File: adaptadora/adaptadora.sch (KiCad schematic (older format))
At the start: 34 parts

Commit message: add files, libs, sch videos, sch sincronismo
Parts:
- removed C? (x8): 100n, symbol Device:C
- removed J? (x4): Conn_01x32_MountingPin, symbol Connector_Generic_MountingPin:Conn_01x32_MountingPin
- removed J?: Conn_02x10_Odd_Even, symbol Connector_Generic:Conn_02x10_Odd_Even
- removed JP? (x8): SolderJumper_3_Open, symbol Jumper:SolderJumper_3_Open
- removed RN? (x2): CAT16-153J8LF, CAT16104J4LF, symbol adaptadora-rescue:CAT16-153J8LF-CAT16-153J8LF
- removed U? (x4): SN74LVC2T45DCTR, DCT8, symbol adaptadora-rescue:SN74LVC2T45DCTR-2019-09-10_15-53-16-SH-rescue
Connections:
- net labels removed: ALT_0, ALT_1, ALT_2, ALT_3, ALT_4, ALT_5, ALT_6, ALT_7, GO_PULSE, PBRES, PBRES_EDU-CIAA, SPARE_1, SPARE_2, TIMEMARK, TIMEMARK_EDU-CIAA, TRIGG_SEC, TXA, TXA_EDU-CIAA, VIDEO_COMP, VIDEO_PRIM, ZRT
- wire segments 58 -> 0
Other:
- note removed: "FATA LO QUE VA A LA FPGA"
- note removed: "GPS"
- note removed: "LO DE ESTE LADO VA AL uC"
- note removed: "PE1A"
- note removed: "PE1B"
- note removed: "PE2A"
- note removed: "PE2B"
- note removed: "PEINE96"
- note removed: "TRANSLATORS"
- moved on the sheet: J?

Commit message: add files
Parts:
- removed J?: Conn_02x17_Odd_Even, symbol Connector_Generic:Conn_02x17_Odd_Even
- added C? (x7): C, symbol Device:C
- added C? (x4): CP1, symbol Device:CP1
- added D? (x3): D_TVS, symbol Device:D_TVS
- added J? (x7): Conn_Coaxial, symbol Connector:Conn_Coaxial
- added JP? (x4): Jumper_3_Open, symbol Jumper:Jumper_3_Open
- added R? (x3): R, symbol Device:R
- added RV? (x4): R_POT, symbol Device:R_POT
- added U?: TLV2772IDR, SOIC127P600X175-8N, symbol TLV2772IDR:TLV2772IDR
- added U?: LM361MX_NOPB-LM361MX_NOPB, SOIC127P600X175-14N, symbol sincronismo-rescue:LM361MX_NOPB-LM361MX_NOPB
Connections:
- net labels added: +12V, +5V, -12V, ACP_3P3, ARP_3P3, PRF_3P3, VIDEO_DIGITAL, V_COMP, V_COMP_3P3
- net labels removed: ACP, ACP_FPGA, ARP, ARP_FPGA, JMP1_FPGA, JMP2_FPGA, JMP3_FPGA, JMP4_FPGA, JMP5_FPGA, JMP6_FPGA, JMP7_FPGA, JMP8_FPGA, PRF, PRF_FPGA, VIDEO_COMP_FPGA, VIDEO_PRIM_FPGA
- wire segments 0 -> 144
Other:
- note removed: "DAC"
- note removed: "EDU-CIAA"
- note removed: "FALTA LA HUELLA DE LOS CAPACITORES Y LAS HUELLAS DE TODO NOMAS"
- note removed: "FPGA"
- moved on the sheet: J?

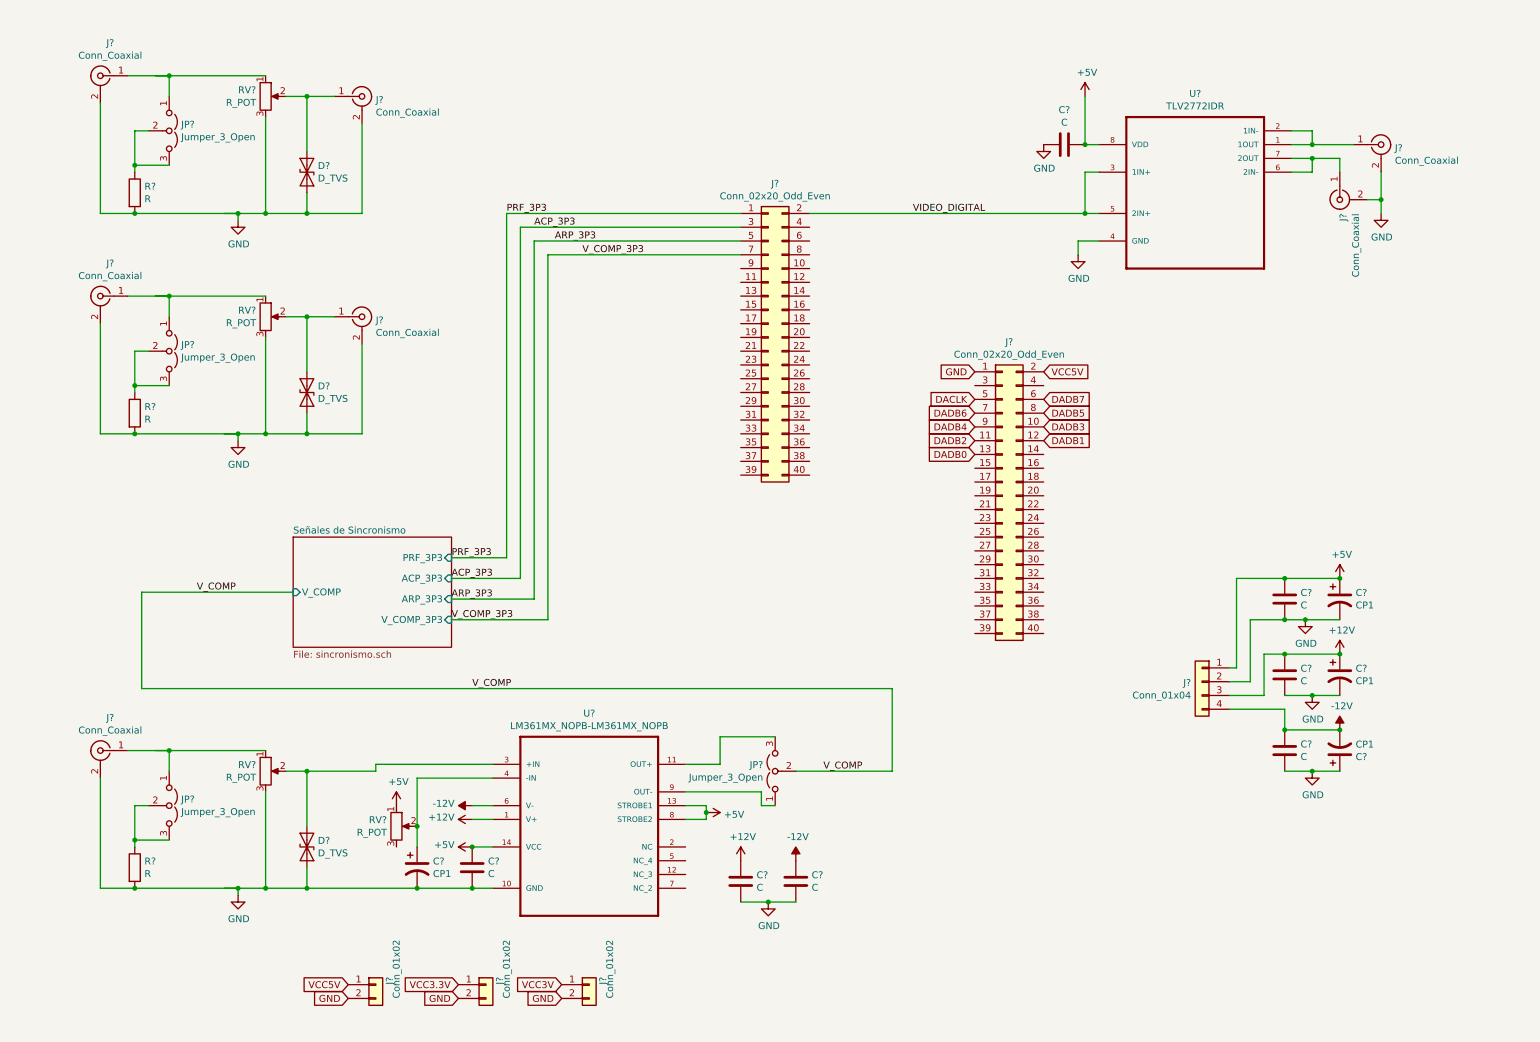
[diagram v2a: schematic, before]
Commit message: esquemático terminado faltan valores
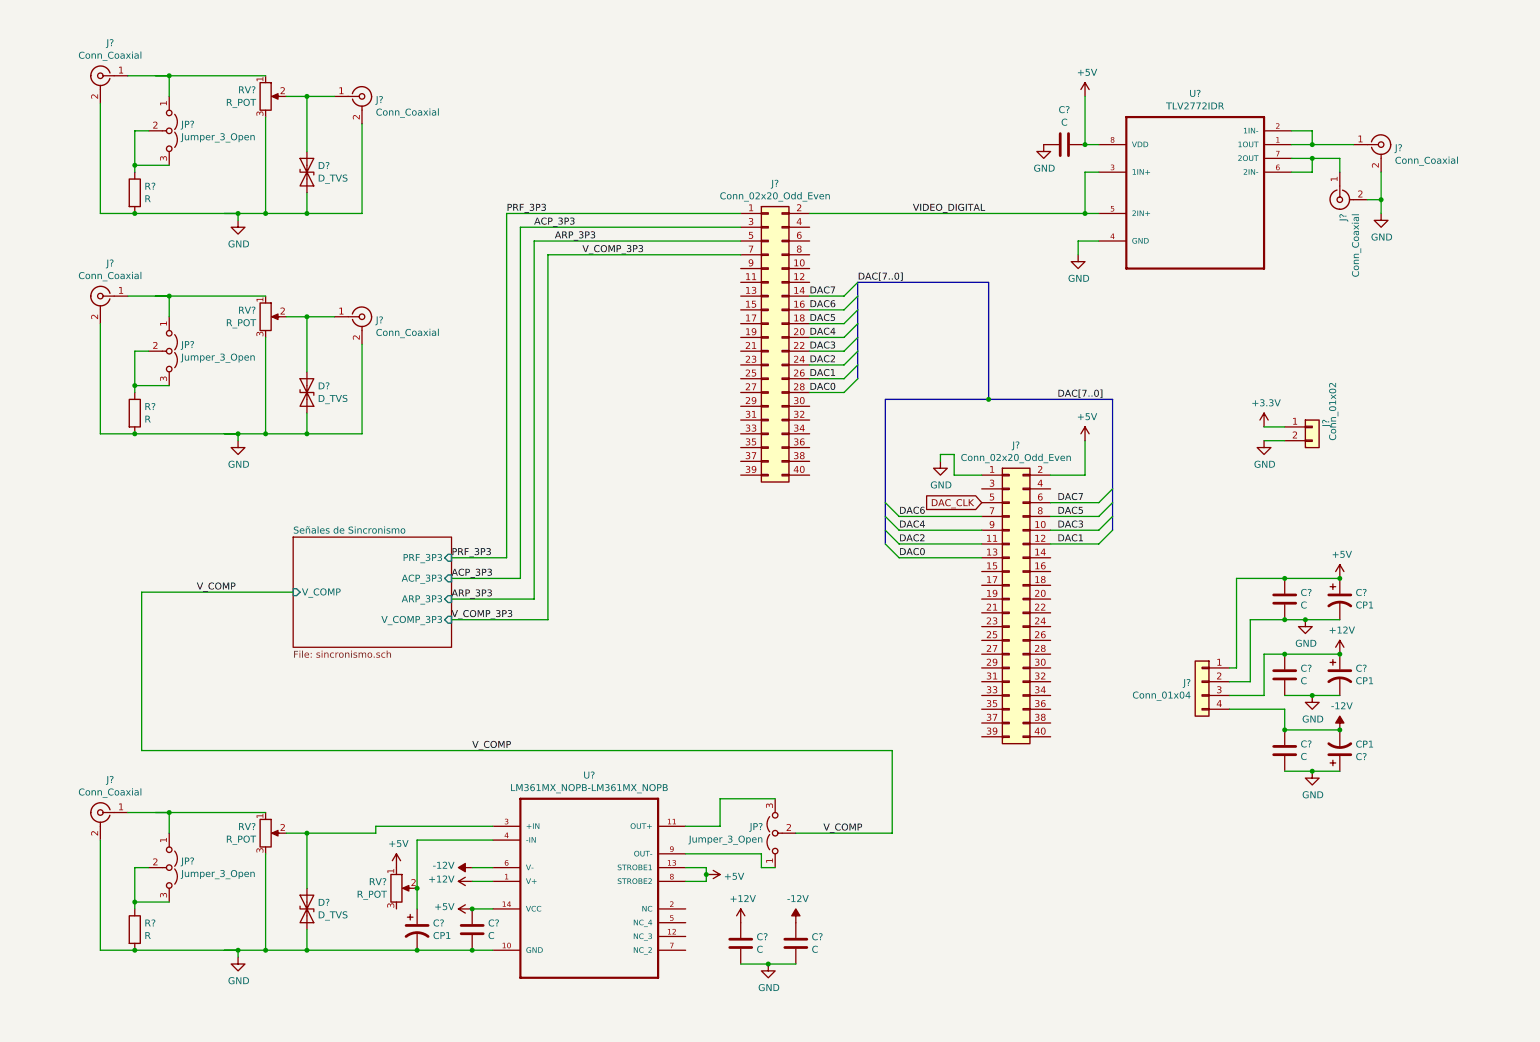
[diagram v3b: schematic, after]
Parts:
- removed J? (x2): Conn_01x02, symbol Connector_Generic:Conn_01x02
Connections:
- net labels added: +3.3V, DAC0, DAC1, DAC2, DAC3, DAC4, DAC5, DAC6, DAC7, DAC[7..0], DAC_CLK
- net labels removed: DACLK, DADB0, DADB1, DADB2, DADB3, DADB4, DADB5, DADB6, DADB7, VCC3.3V, VCC3V, VCC5V
- wire segments 144 -> 168
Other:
- moved on the sheet: C?, D?, J?, JP?, R?, RV?, U?

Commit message: se enumeraron componentes faltan valores
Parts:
- added J6: Conn_01x02, symbol Connector_Generic:Conn_01x02
- gave numbers to parts that had none: 38
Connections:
- wire segments 168 -> 173

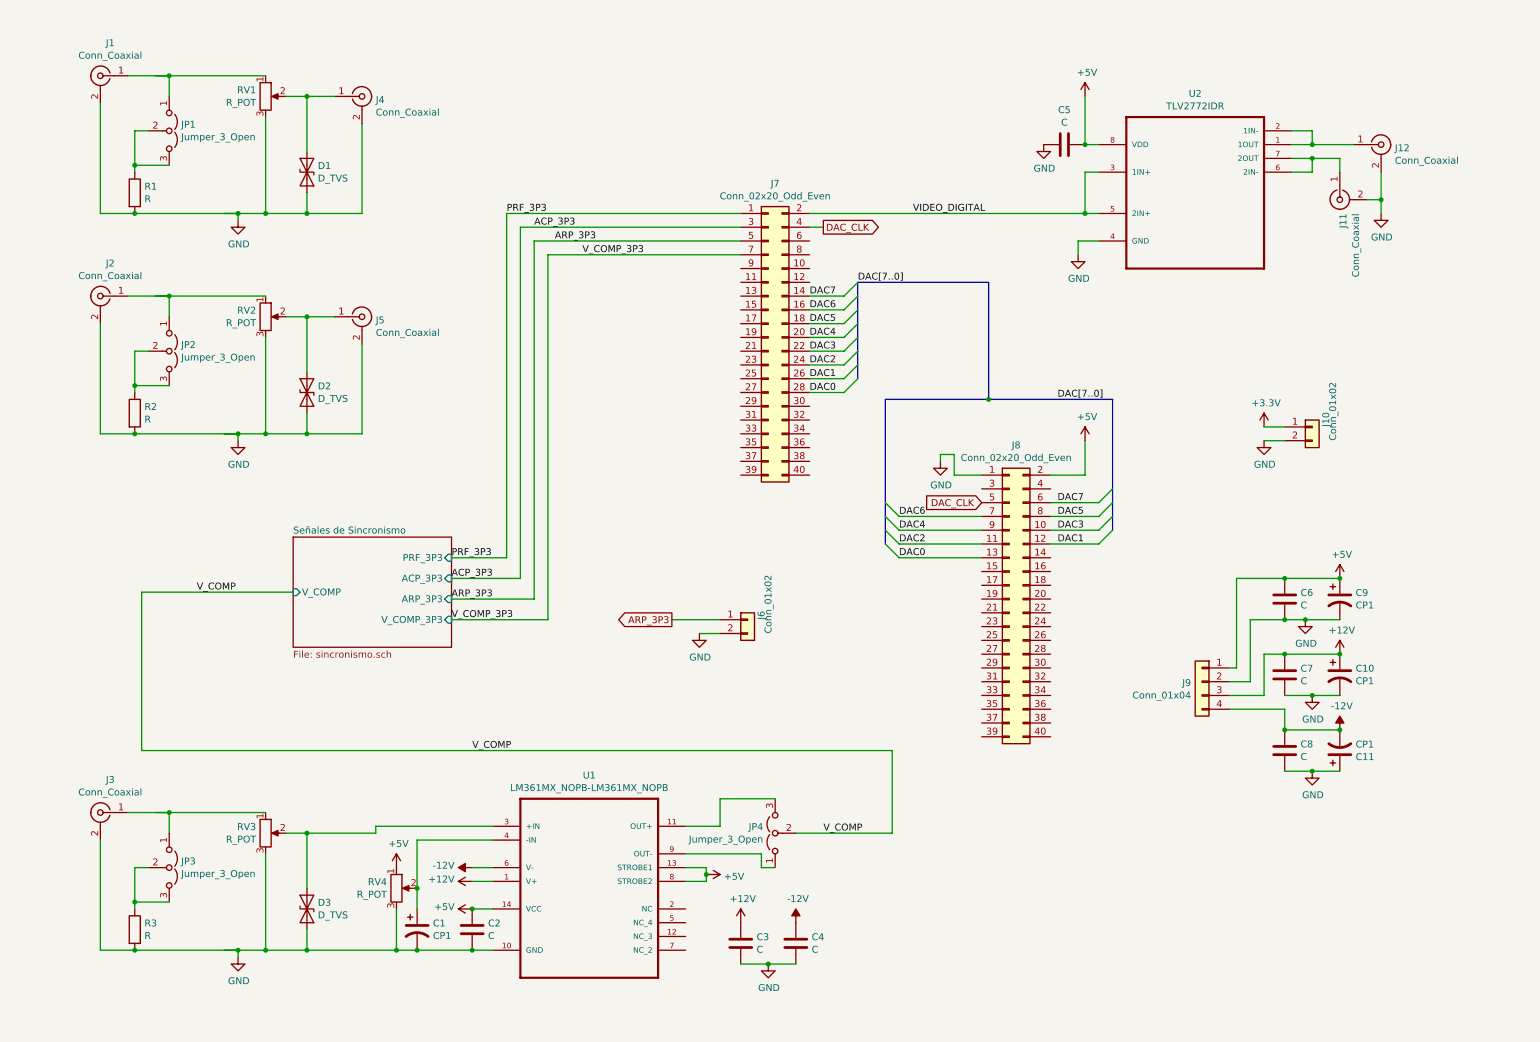
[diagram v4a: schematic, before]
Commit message: se agregan valores, etiquetas jerarquicas y poligonos
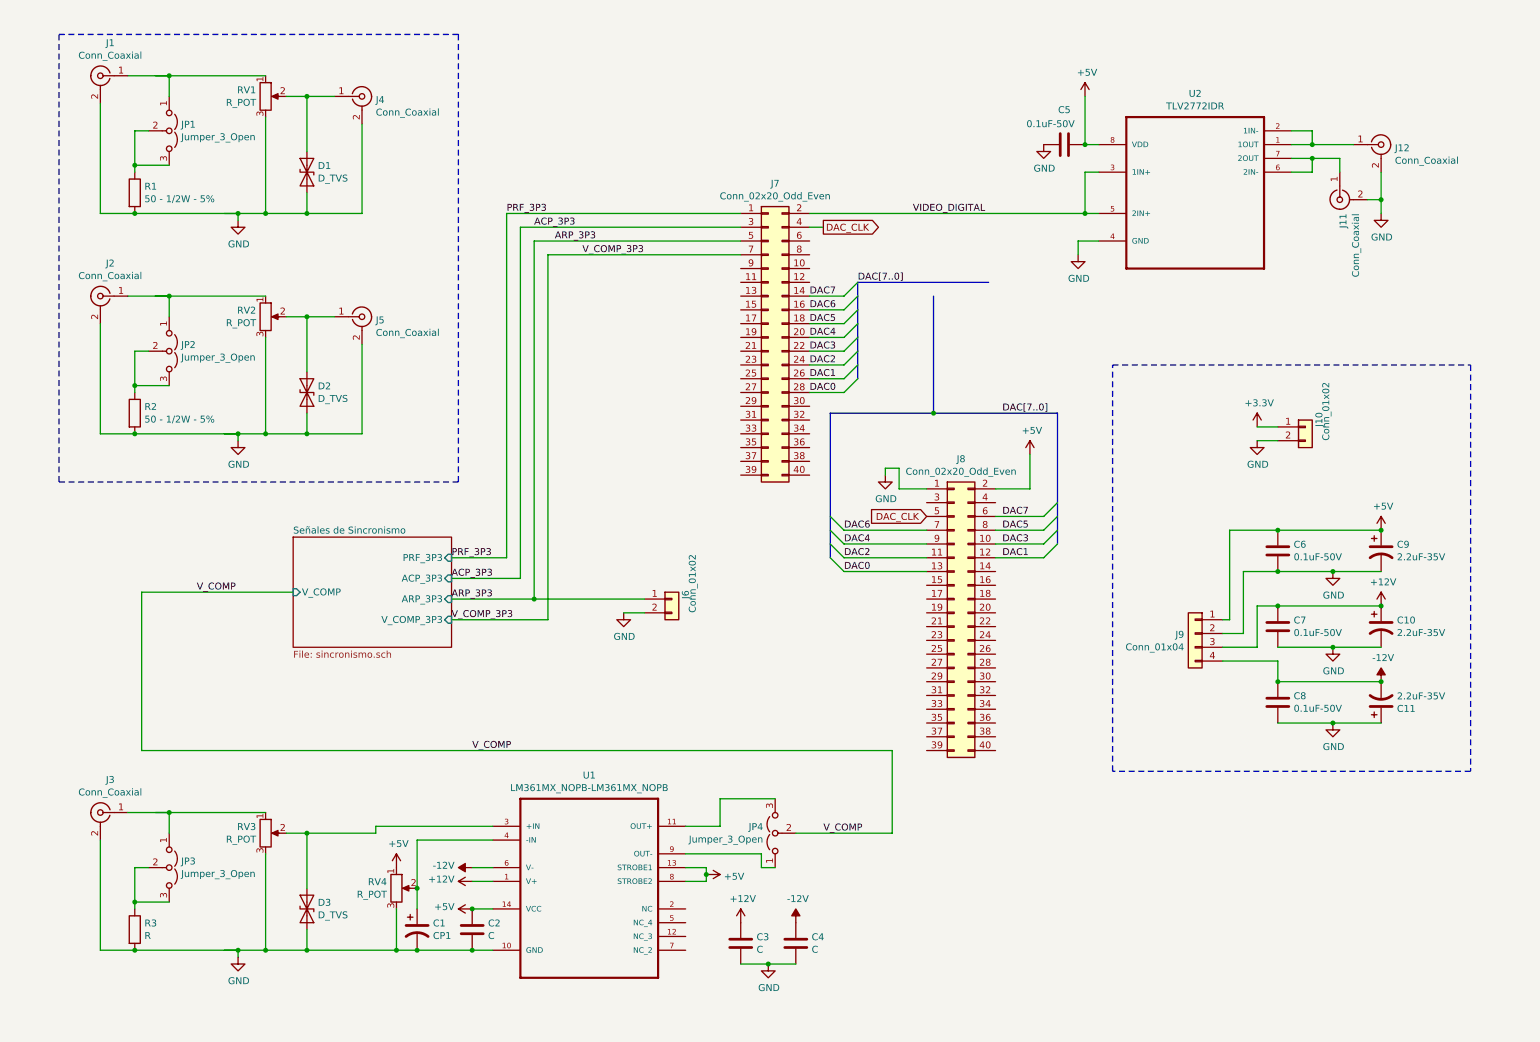
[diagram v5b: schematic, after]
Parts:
- C10, C11, C9: value CP1 -> 2.2uF-35V
- C5, C6, C7, C8: value C -> 0.1uF-50V
- R1, R2: value R -> 50 - 1/2W - 5%
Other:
- moved on the sheet: C10, C11, C6, C7, C8, C9, J10, J6, J8, J9

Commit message: se agrega texto
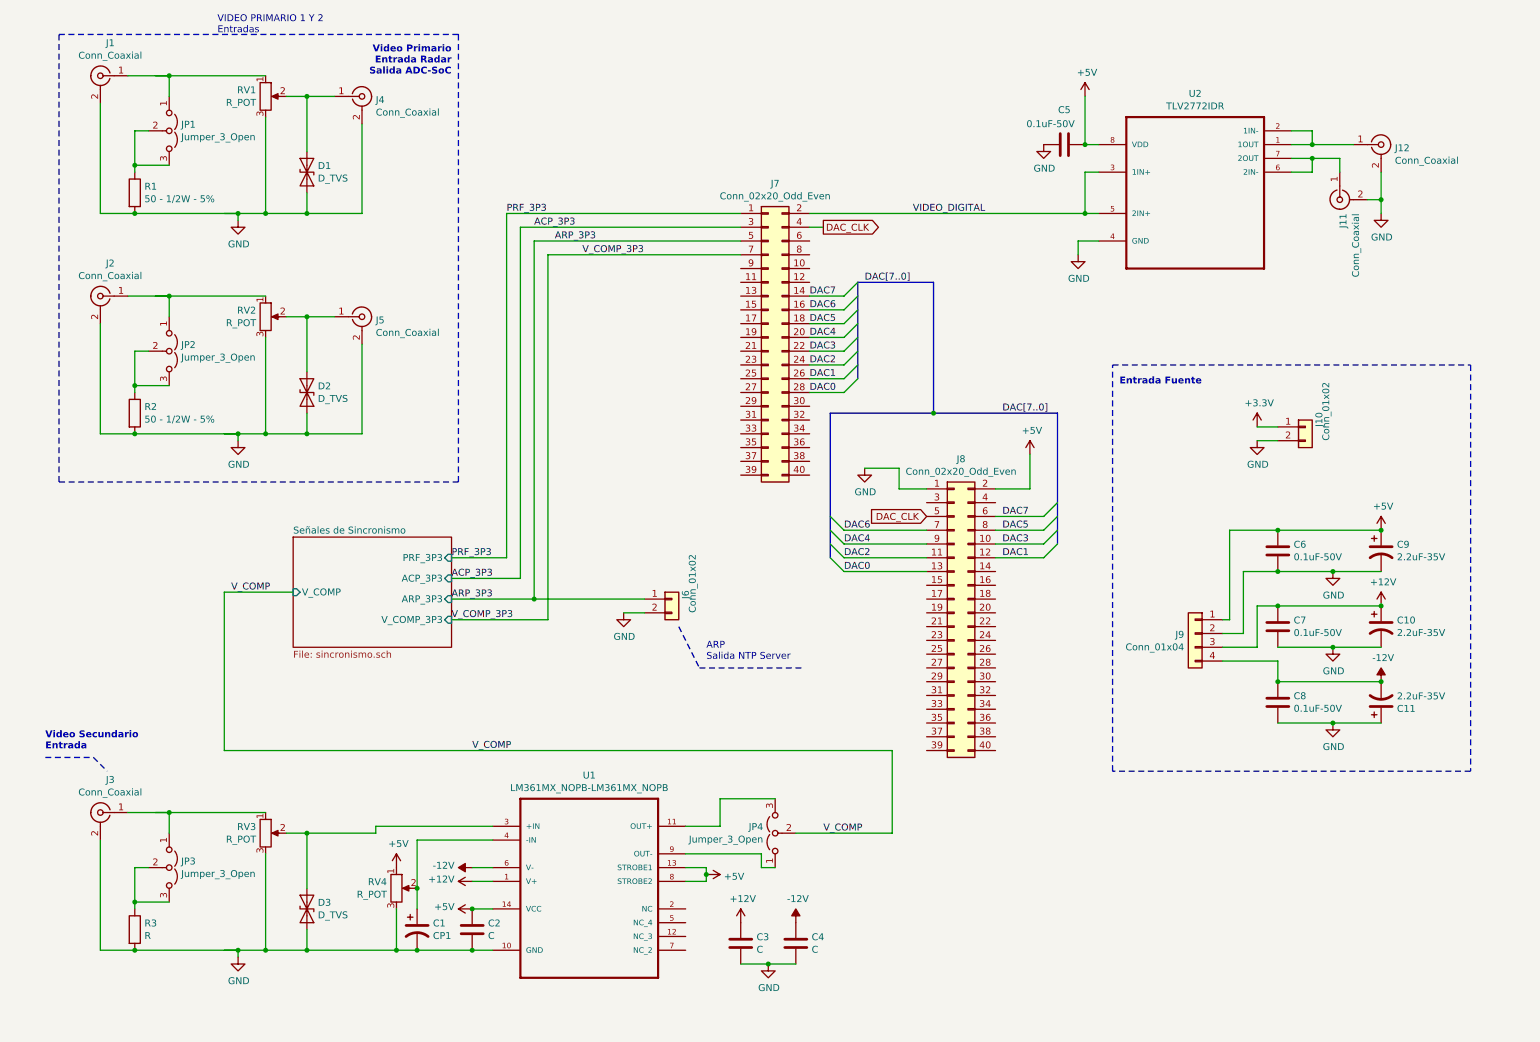
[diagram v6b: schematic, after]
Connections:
- wire segments 173 -> 172
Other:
- note added: "ARP\nSalida NTP Server"
- note added: "Entrada Fuente"
- note added: "VIDEO PRIMARIO 1 Y 2\nEntradas"
- note added: "Video Primario\nEntrada Radar\nSalida ADC-SoC"
- note added: "Video Secundario\nEntrada"
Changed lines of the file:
@@
 	6750 6400 6750 5800
 Wire Wire Line
-	6750 5800 1300 5800
-Wire Wire Line
-	1300 5800 1300 4650
+	6750 5800 1900 5800
+Wire Wire Line
+	1900 5800 1900 4650
 Wire Wire Line
 	6050 6400 6750 6400
 Wire Wire Line
-	1300 4650 2400 4650
+	1900 4650 2400 4650
 Text Label 6250 6400 0    50   ~ 0
 V_COMP
 Text Label 3700 5800 0    50   ~ 0
 V_COMP
-Text Label 1700 4650 0    50   ~ 0
+Text Label 1950 4650 0    50   ~ 0
 V_COMP
 Text Label 6900 1900 0    50   ~ 0
@@
 L power:GND #PWR013
 U 1 1 5DAF1F2B
-P 6700 3800
-F 0 "#PWR013" H 6700 3550 50  0001 C CNN
-F 1 "GND" H 6705 3627 50  0000 C CNN
-F 2 "" H 6700 3800 50  0001 C CNN
-F 3 "" H 6700 3800 50  0001 C CNN
-	1    6700 3800
+P 6550 3750
+F 0 "#PWR013" H 6550 3500 50  0001 C CNN
+F 1 "GND" H 6555 3577 50  0000 C CNN
+F 2 "" H 6550 3750 50  0001 C CNN
+F 3 "" H 6550 3750 50  0001 C CNN
+	1    6550 3750
 	1    0    0    -1
 $EndComp
@@
 	7750 3900 7750 3650
 Wire Wire Line
-	6700 3800 6700 3750
-Wire Wire Line
 	6800 3750 6800 3900
 Wire Wire Line
 	6800 3900 7000 3900
-Wire Wire Line
-	6700 3750 6800 3750
 Text GLabel 7000 4100 0    50   Input ~ 0
 DAC_CLK
@@
 	6400 2500 6500 2400
 Wire Bus Line
-	6500 2400 7450 2400
-Text Label 6500 2400 0    50   ~ 0
+	6500 2400 7050 2400
+Text Label 6550 2400 0    50   ~ 0
 DAC[7..0]
-Wire Bus Line
-	7050 2500 7050 3350
 Connection ~ 7050 3350
 Wire Bus Line
@@
 Wire Notes Line
 	3600 600  3600 3850
+Text Notes 1850 600  0    0    ~ 0
+VIDEO PRIMARIO 1 Y 2\nEntradas
+Text Notes 3550 900  2    50   ~ 10
+Video Primario\nEntrada Radar\nSalida ADC-SoC
+Text Notes 8400 3150 0    50   ~ 10
+Entrada Fuente
+Text Notes 600  5800 0    50   ~ 10
+Video Secundario\nEntrada
+Wire Notes Line
+	950  5850 1050 5950
+Wire Notes Line
+	600  5850 950  5850
+Wire Notes Line
+	5200 4900 5350 5200
+Text Notes 5400 5150 0    50   ~ 0
+ARP\nSalida NTP Server
+Wire Notes Line
+	5350 5200 6100 5200
+Wire Bus Line
+	7050 2400 7050 3350
+Wire Wire Line
+	6550 3750 6800 3750
 Wire Bus Line
 	6300 3350 6300 4400
